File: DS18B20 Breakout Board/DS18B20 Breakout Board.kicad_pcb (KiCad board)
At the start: 2 copper layers, 25 x 8 mm, 3 parts, among them J1 Conn_01x02_Socket, J2 Conn_01x02_Socket, U1 DS18B20

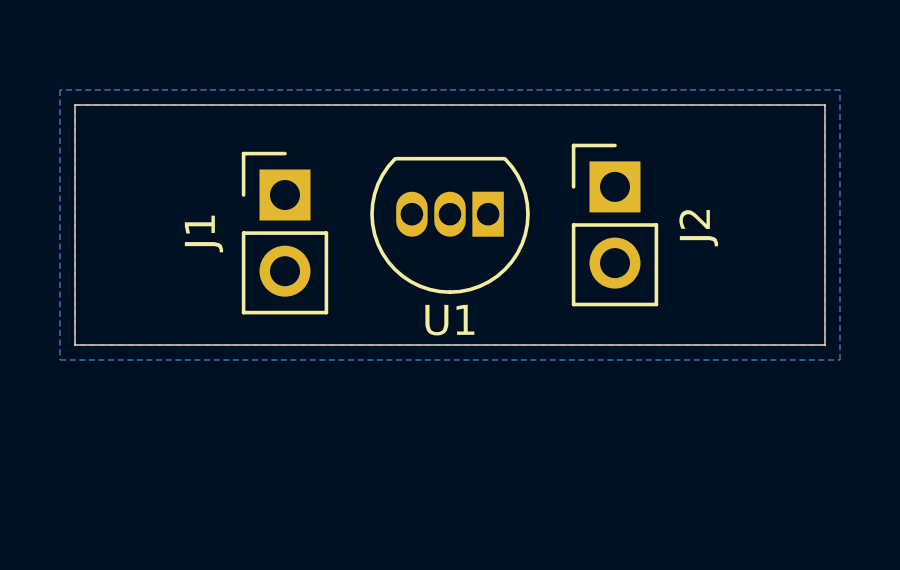
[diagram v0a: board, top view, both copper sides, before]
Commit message: reconfigure DS18B20 breakout board
- Change JST from 2-pin to 3-pin
- Add a solder jumper for switching between parasitic and external power
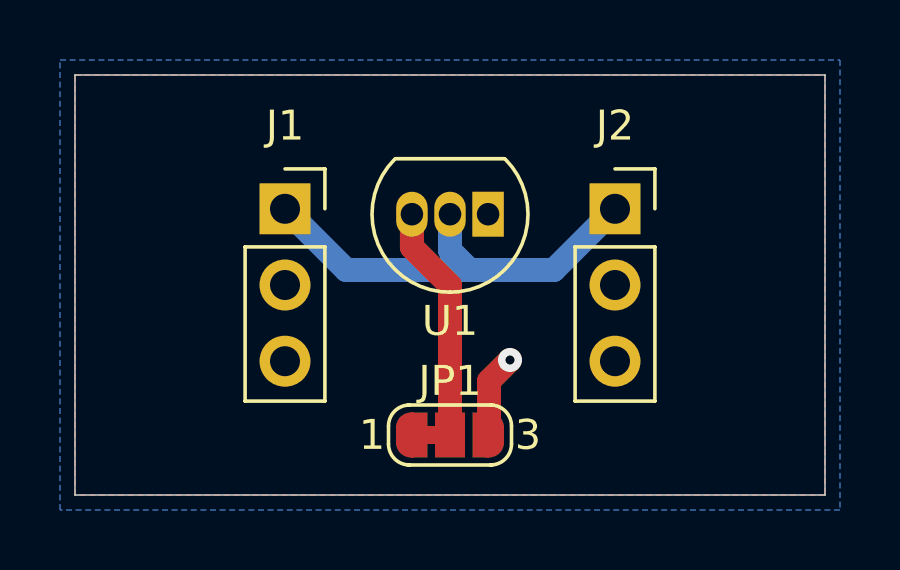
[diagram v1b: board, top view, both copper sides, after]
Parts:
- added JP1: SolderJumper_3_Bridged12, Jumper:SolderJumper-3_P1.3mm_Bridged12_RoundedPad1.0x1.5mm_NumberLabels, F.Cu at (90.5, 43.0)
- J1, J2: value Conn_01x02_Socket -> Conn_01x03_Socket; footprint Connector_PinHeader_2.54mm:PinHeader_1x02_P2.54mm_Vertical -> Connector_PinSocket_2.54mm:PinSocket_1x03_P2.54mm_Vertical
- moved J2 0.73 mm to (96.0, 35.5)
- moved J1 0.46 mm to (85.0, 35.5)
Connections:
- J1 pad 2: GND -> +3V3
- J2 pad 2: GND -> +3V3
- U1 pad 3: GND -> Net-(JP1-C)
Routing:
- net /Data_Line: track 0.00 -> 16.7 mm
- net Net-(JP1-C): track 0.00 -> 7.89 mm
- net +3V3: track 0.00 -> 2.79 mm, vias 0 -> 1
- added copper zone on B.Cu, net +3V3
- added copper zone on F.Cu, net GND
- removed copper zone on F.Cu, net /Data_Line
- removed copper zone on B.Cu, net GND
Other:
- board size 25 x 8 mm -> 25 x 14 mm
